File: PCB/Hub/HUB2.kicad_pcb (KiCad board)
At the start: 2 copper layers, 98.8 x 85.2 mm, 31 parts, among them IC1 ESP32-DEVKITC-VE, IC2 TCAN1051VDRQ1, J1 B4B-PH-SM4-TB, K1 DSY2Y-S-205H, Q2 2N2220, U1 BMP581, U10 DB301V-5.0-2P, U3 DB301V-5.0-2P, U4 DB301V-5.0-2P, U5 BMI088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

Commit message: gbr
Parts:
- moved R3 3.67 mm to (109.8, 87.5)
- moved Q2 3.04 mm to (93.5, 90.0)
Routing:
- net Net-(IC1-RX): track 86.3 -> 101.9 mm
- net Net-(IC1-IO2): track 76.5 -> 85.6 mm
- net +5V: track 114.4 -> 122.3 mm
- net Net-(IC1-TX): track 89.1 -> 96.7 mm
- net Net-(IC1-IO4): track 31.2 -> 36.8 mm
- net Net-(D1-A): track 23.9 -> 21.8 mm
- net Net-(Q2-B): track 4.30 -> 3.67 mm

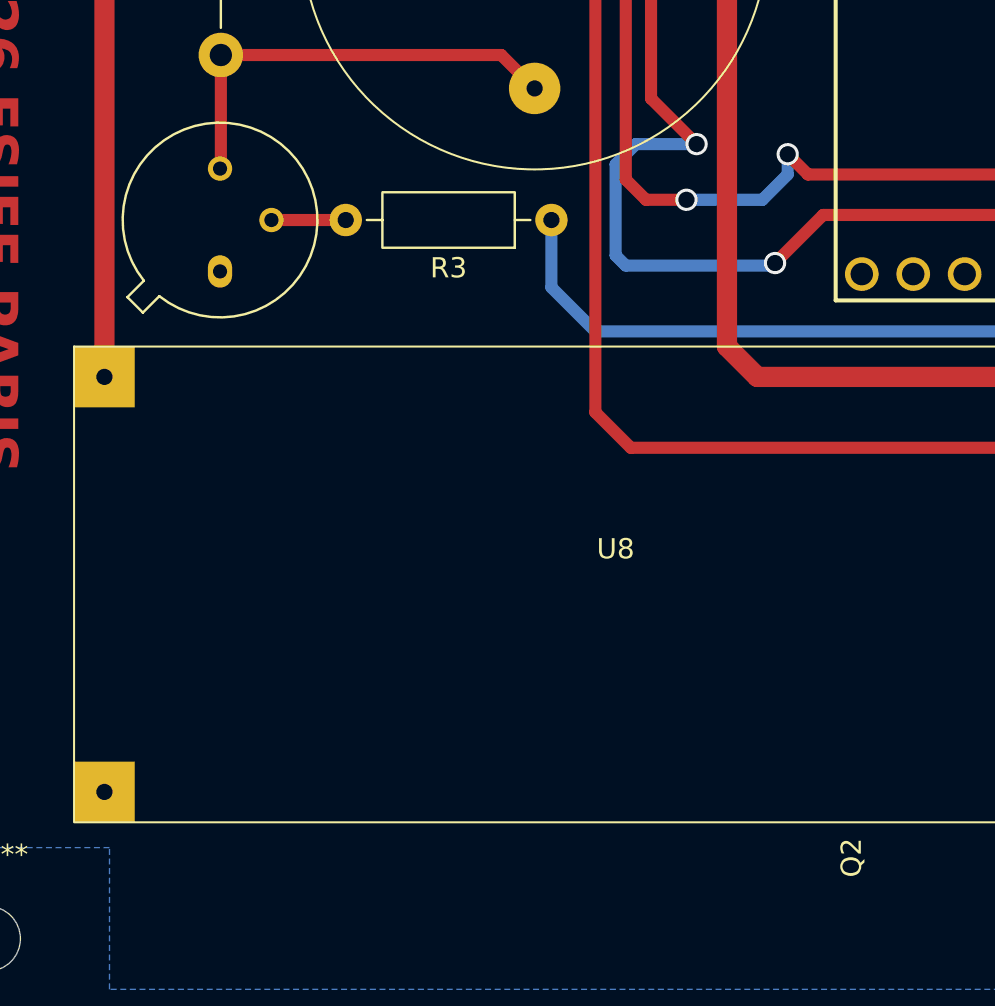
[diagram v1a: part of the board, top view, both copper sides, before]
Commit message: changement transistor 2N2222 (empreinte)
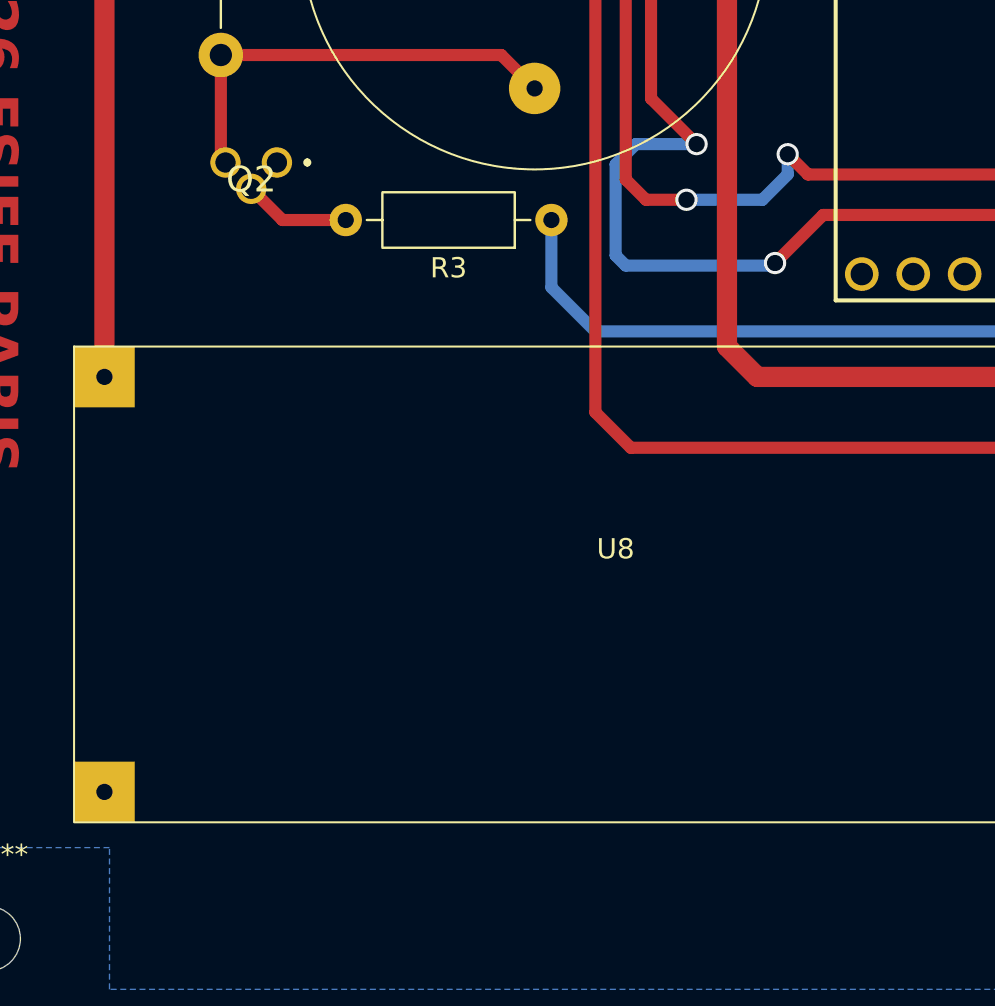
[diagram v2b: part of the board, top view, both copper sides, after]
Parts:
- Q2: value 2N2220 -> 2N2222; footprint Package_TO_SOT_THT:TO-39-3 -> Bibliotheque_Projet:2N2222B
- moved Q2 6.07 mm to (96.3, 84.7), turned to 180 degrees
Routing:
- net Net-(Q2-B): track 3.67 -> 5.31 mm
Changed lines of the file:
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@@
 		)
 	)
-	(footprint "Package_TO_SOT_THT:TO-39-3"
+	(footprint "Bibliotheque_Projet:2N2222B"
 		(layer "F.Cu")
-		(at 93.46 90.04 90)
-		(descr "TO-39-3")
-		(tags "TO-39-3")
+		(at 96.27 84.658 180)
+		(descr "TO−92 3 4.825x4.76 CASE 135AN ISSUE O")
+		(tags "Transistor BJT NPN")
 		(property "Reference" "Q2"
-			(at -28.96 31.19 90)
+			(at 1.27 -0.842 0)
 			(layer "F.SilkS")
 			(effects
 				(font
+					(size 1.27 1.27)
+					(thickness 0.254)
+				)
+			)
+		)
+		(property "Value" "2N2222"
+			(at 1.27 -0.842 0)
+			(layer "F.SilkS")
+			(hide yes)
+			(effects
+				(font
+					(size 1.27 1.27)
+					(thickness 0.254)
+				)
+			)
+		)
+		(property "Datasheet" "https://diotec.com/request/datasheet/2n2222a.pdf"
+			(at 0 0 0)
+			(layer "F.Fab")
+			(hide yes)
+			(effects
+				(font
+					(size 1.27 1.27)
+				)
+			)
+		)
+		(property "Description" "NPN General purpose transistor . IC 150 mA . f 	100 MHz"
+			(at 0 0 0)
+			(layer "F.Fab")
+			(hide yes)
+			(effects
+				(font
+					(size 1.27 1.27)
+				)
+			)
+		)
+		(property "Sim.Device" "NPN"
+			(at 0 0 180)
+			(unlocked yes)
+			(layer "F.Fab")
+			(hide yes)
+			(effects
+				(font
 					(size 1 1)
 					(thickness 0.15)
@@
 			)
 		)
-		(property "Value" "2N2220"
-			(at 2.54 5.81 90)
+		(property "Sim.Pins" "1=E 2=B 3=C"
+			(at 0 0 180)
+			(unlocked yes)
 			(layer "F.Fab")
+			(hide yes)
 			(effects
 				(font
@@
 			)
 		)
-		(property "Datasheet" "http://www.onsemi.com/pub_link/Collateral/2N2219-D.PDF"
-			(at 0 0 90)
+		(property "Height" "7.5"
+			(at 0 0 180)
+			(unlocked yes)
 			(layer "F.Fab")
 			(hide yes)
 			(effects
 				(font
-					(size 1.27 1.27)
+					(size 1 1)
+					(thickness 0.15)
 				)
 			)
 		)
-		(property "Description" "800mA Ic, 50V Vce, NPN Transistor, TO-39"
-			(at 0 0 90)
+		(property "Mouser Part Number" "637-2N2222A"
+			(at 0 0 180)
+			(unlocked yes)
 			(layer "F.Fab")
 			(hide yes)
 			(effects
 				(font
-					(size 1.27 1.27)
+					(size 1 1)
+					(thickness 0.15)
 				)
 			)
 		)
-		(property "KiLib_Generator" "package/TO_SOT/THT"
-			(at 0 0 90)
-			(layer "F.SilkS")
+		(property "Mouser Price/Stock" "https://www.mouser.co.uk/ProductDetail/Diotec-Semiconductor/2N2222A?qs=OlC7AqGiEDmNlRSTGL2dYg%3D%3D"
+			(at 0 0 180)
+			(unlocked yes)
+			(layer "F.Fab")
 			(hide yes)
 			(effects
@@
 			)
 		)
-		(property "Sim.Device" "NPN"
-			(at 0 0 90)
+		(property "Manufacturer_Name" "Diotec"
+			(at 0 0 180)
 			(unlocked yes)
 			(layer "F.Fab")
@@
 			)
 		)
-		(property "Sim.Pins" "1=E 2=B 3=C"
-			(at 0 0 90)
+		(property "Manufacturer_Part_Number" "2N2222A"
+			(at 0 0 180)
 			(unlocked yes)
 			(layer "F.Fab")
@@
 			)
 		)
-		(property ki_fp_filters "TO?39*")
 		(sheetname "/")
 		(sheetfile "HUB2.kicad_sch")
@@
 		(duplicate_pad_numbers_are_jumpers no)
 		(fp_line
-			(start -1.271018 -4.574693)
-			(end -2.034693 -3.811018)
+			(start -1.5 0.1)
+			(end -1.5 0.1)
 			(stroke
-				(width 0.12)
+				(width 0.2)
 				(type solid)
 			)
@@
 		)
 		(fp_line
-			(start -2.034693 -3.811018)
-			(end -1.22152 -2.997844)
+			(start -1.5 -0.1)
+			(end -1.5 -0.1)
 			(stroke
-				(width 0.12)
+				(width 0.2)
 				(type solid)
 			)
 			(layer "F.SilkS")
 		)
-		(fp_line
-			(start -0.457844 -3.76152)
-			(end -1.271018 -4.574693)
+		(fp_arc
+			(start -1.5 0.1)
+			(mid -1.6 0)
+			(end -1.5 -0.1)
 			(stroke
-				(width 0.12)
+				(width 0.2)
 				(type solid)
 			)
@@
 		)
 		(fp_arc
-			(start -0.457844 -3.76152)
-			(mid 5.941184 3.401184)
-			(end -1.22152 -2.997844)
+			(start -1.5 -0.1)
+			(mid -1.4 0)
+			(end -1.5 0.1)
 			(stroke
-				(width 0.12)
+				(width 0.2)
 				(type solid)
 			)
@@
 		)
 		(fp_line
-			(start -1.269834 -4.771499)
-			(end -2.231499 -3.809834)
+			(start 4.514 2)
+			(end -1.974 2)
 			(stroke
-				(width 0.05)
+				(width 0.1)
 				(type solid)
 			)
@@
 		)
 		(fp_line
-			(start -0.446162 -3.947827)
-			(end -1.269834 -4.771499)
+			(start 4.514 -3.684)
+			(end 4.514 2)
 			(stroke
-				(width 0.05)
+				(width 0.1)
 				(type solid)
 			)
@@
 		)
 		(fp_line
-			(start -2.231499 -3.809834)
-			(end -1.407827 -2.986162)
+			(start -1.974 2)
+			(end -1.974 -3.684)
 			(stroke
-				(width 0.05)
+				(width 0.1)
 				(type solid)
 			)
 			(layer "F.CrtYd")
 		)
-		(fp_arc
-			(start -0.446162 -3.947827)
-			(mid 6.040179 3.500179)
-			(end -1.407827 -2.986162)
+		(fp_line
+			(start -1.974 -3.684)
+			(end 4.514 -3.684)
 			(stroke
-				(width 0.05)
+				(width 0.1)
 				(type solid)
 			)
@@
 		)
 		(fp_line
-			(start -1.27151 -4.419621)
-			(end -1.879621 -3.81151)
+			(start 3.47 0)
+			(end 3.47 0)
 			(stroke
 				(width 0.1)
@@
 		)
 		(fp_line
-			(start -1.879621 -3.81151)
-			(end -1.07352 -3.005408)
+			(start 3.27 1)
+			(end 3.47 0)
 			(stroke
 				(width 0.1)
@@
 		)
 		(fp_line
-			(start -0.465408 -3.61352)
-			(end -1.27151 -4.419621)
+			(start -0.73 1)
+			(end 3.27 1)
 			(stroke
 				(width 0.1)
@@
 			(layer "F.Fab")
 		)
-		(fp_arc
-			(start -0.465408 -3.61352)
-			(mid 5.863402 3.323402)
-			(end -1.07352 -3.005408)
+		(fp_line
+			(start -0.93 0)
+			(end -0.73 1)
 			(stroke
 				(width 0.1)
@@
 			(layer "F.Fab")
 		)
-		(fp_circle
-			(center 2.54 0)
-			(end 6.79 0)
+		(fp_arc
+			(start -0.930152 -0.000763)
+			(mid 1.270389 -2.683568)
+			(end 3.47 0)
 			(stroke
 				(width 0.1)
 				(type solid)
 			)
-			(fill no)
 			(layer "F.Fab")
 		)
 		(fp_text user "${REFERENCE}"
-			(at -28.96 31.19 90)
+			(at 1.27 -0.842 0)
 			(layer "F.Fab")
 			(effects
 				(font
-					(size 1 1)
-					(thickness 0.15)
+					(size 1.27 1.27)
+					(thickness 0.254)
 				)
 			)
 		)
-		(pad "1" thru_hole oval
-			(at 0 0 90)
-			(size 1.6 1.2)
-			(drill 0.7)
+		(pad "1" thru_hole circle
+			(at 0 0 180)
+			(size 1.5 1.5)
+			(drill 1)
 			(layers "*.Cu" "*.Mask")
 			(remove_unused_layers no)
@@
 		)
 		(pad "2" thru_hole circle
-			(at 2.54 2.54 90)
-			(size 1.2 1.2)
-			(drill 0.7)
+			(at 1.27 -1.3 180)
+			(size 1.5 1.5)
+			(drill 1)
 			(layers "*.Cu" "*.Mask")
 			(remove_unused_layers no)
 			(net "Net-(Q2-B)")
 			(pinfunction "B_2")
-			(pintype "input")
+			(pintype "passive")
 		)
 		(pad "3" thru_hole circle
-			(at 5.08 0 90)
-			(size 1.2 1.2)
-			(drill 0.7)
+			(at 2.54 0 180)
+			(size 1.5 1.5)
+			(drill 1)
 			(layers "*.Cu" "*.Mask")
 			(remove_unused_layers no)
@@
 		)
 		(embedded_fonts no)
-		(model "${KICAD10_3DMODEL_DIR}/Package_TO_SOT_THT.3dshapes/TO-39-3.step"
+		(model "2N3904BU.stp"
 			(offset
-				(xyz 0 0 0)
+				(xyz 1.269999962 -0.1099999978 3.440000006)
 			)
 			(scale
@@
 			)
 			(rotate
-				(xyz 0 0 0)
+				(xyz 90 0 0)
 			)
 		)
@@
 	)
 	(segment
-		(start 96 87.5)
-		(end 99.67 87.5)
+		(start 96.542 87.5)
+		(end 95 85.958)
+		(width 0.6)
+		(layer "F.Cu")
+		(net "Net-(Q2-B)")
+	)
+	(segment
+		(start 99.67 87.5)
+		(end 96.542 87.5)
 		(width 0.6)
 		(layer "F.Cu")

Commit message: MaJ composants Hub empreinte et schematic
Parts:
- IC1: footprint projet:ESP32DEVKITCVE -> Bibliotheque_Projet:ESP32-WROVER DevKitC
- IC2: value TCAN1051VDRQ1 -> Tranceiver_CAN; footprint projet:SOIC127P600X175-8N -> Bibliotheque_Projet:Tranceiver CAN
- J1: value B4B-PH-SM4-TB -> Connecteur_male_Grove_Mabee; footprint projet:CONN_JST -> Bibliotheque_Projet:Connecteur male Grove_Mabee
- JP1: value Jumper -> Jumper CAN Hub; footprint projet:jumper -> Bibliotheque_Projet:Jumper CAN hub
- K1: footprint projet:DSY2YS205L -> Bibliotheque_Projet:Relais DSY2Y-S-205H
- LS1: value Buzzer -> Buzzer 12V; footprint projet:Sans titre -> Bibliotheque_Projet:Buzzer 12V
- U10, U3, U6, U7: value DB301V-5.0-2P -> Bornier_a_vis; footprint projet:CONN-TH_2P-P5.00_L7.6-W10.0 -> Bibliotheque_Projet:Bornier a vis
- U4, U9: footprint projet:CONN-TH_2P-P5.00_L7.6-W10.0 -> Bibliotheque_Projet:Bornier a vis
- U5: footprint projet:BMI088 -> Bibliotheque_Projet:BMI088
- U8: footprint projet:aba -> Bibliotheque_Projet:Abaisseur tension reglable
- moved JP1 7.02 mm to (153.5, 38.7)
- moved J1 2.25 mm to (161.6, 57.5)
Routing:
- net Net-(IC1-IO33): track 22.8 -> 19.0 mm
- net Net-(IC1-IO32): track 18.4 -> 14.6 mm
- net +5V: track 122.3 -> 118.6 mm
